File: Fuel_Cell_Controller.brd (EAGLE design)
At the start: 254 x 152.4 mm, 62 parts, among them U1 MAX232PTH

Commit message: lol kk
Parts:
- removed ETH9: ETHERNET, ETHERNET:A122645-ND
- added ETH5: ETHERNET, ETHERNET:A122645-ND
- J1: value (none) -> BLUETOOTH; device SparkFun-Connectors:1X06 -> FCC_parts:1X06BLUETOOTH
- moved H7 568.4 mm to (10.2, 151.1)
- moved H6 530.2 mm to (83.8, 142.2)
- moved H8 486.0 mm to (7.62, 7.62)
- moved H5 408.6 mm to (83.8, 62.2)
- moved H4 319.7 mm to (83.8, 7.62)
- moved R9 309.7 mm to (144.8, 110.5), turned to 180 degrees
- moved R10 306.4 mm to (139.7, 116.8), turned to 270 degrees
- moved R8 305.3 mm to (148.6, 124.5)
- moved R4 304.1 mm to (165.1, 133.3), turned to 270 degrees
- moved R3 303.7 mm to (165.1, 121.9), turned to 90 degrees
- moved J1 303.0 mm to (154.9, 40.6), turned to 180 degrees
- moved R6 295.2 mm to (148.6, 134.6)
- moved R7 294.1 mm to (142.2, 129.5), turned to 90 degrees
- moved R1 290.8 mm to (144.8, 86.4), turned to 180 degrees
- moved U$16 289.2 mm to (153.7, 116.8), turned to 90 degrees
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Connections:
- removed net AGND: ETH1.P$7, ETH4.P$8, J2.1, U$1.AGND, U$19.P$2, X1.2
- removed net ISC1_SCL: SHTSENSOR.3
- removed net ISC1_SDA: SHTSENSOR.4
- net +5V: now also J1.3; no longer J1.4
- net ESTOP_1: now also ETH5.P$3; no longer ETH6.P$3
- net ESTOP_2: now also ETH5.P$4; no longer ETH6.P$4
- net FAN1_PWR: now also ETH6.P$1; no longer ETH7.P$1
- net FAN2_PWR: now also ETH6.P$4; no longer ETH7.P$4
- net FAN3_PWR: now also ETH7.P$1; no longer ETH8.P$1
- net FROM_BLUE: now also J1.4; no longer J1.3
- net GND: now also ETH1.P$7, ETH4.P$8, ETH5.P$13, ETH5.P$14, ETH5.P$5, ETH5.P$6, ETH5.P$7, ETH5.P$8, ETH8.P$2, ETH8.P$4, ETH8.P$6, J1.1, J2.1, U$1.AGND, U$19.P$2, X1.2; no longer ETH6.P$5, ETH6.P$6, ETH6.P$7, ETH9.P$13, ETH9.P$14, ETH9.P$2, ETH9.P$4, ETH9.P$6, ETH9.P$8, J1.6
- net H2_OK: now also ETH5.P$2; no longer ETH6.P$2
- net I2C1_SCL: now also SHTSENSOR.3
- net I2C1_SDA: now also SHTSENSOR.4
- net OUTPUT_1_ENET: now also ETH8.P$5; no longer ETH9.P$5
- net OUTPUT_2_ENET: now also ETH8.P$7; no longer ETH9.P$7
- net PURGE_VALVE_ENET: now also ETH8.P$3; no longer ETH9.P$3
- net PWM_1: now also ETH6.P$3; no longer ETH7.P$3
- net PWM_2: now also ETH6.P$6; no longer ETH7.P$6
- net PWM_3: now also ETH7.P$3; no longer ETH8.P$3
- net STOP: now also ETH5.P$1; no longer ETH6.P$1
- net SUPPLY_VALVE_ENET: now also ETH8.P$1; no longer ETH9.P$1
- net TACH_1: now also ETH6.P$2; no longer ETH7.P$2
- net TACH_2: now also ETH6.P$5; no longer ETH7.P$5
- net TACH_3: now also ETH7.P$2; no longer ETH8.P$2
- net TO_BLUE: now also J1.5; no longer J1.2
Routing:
- added copper zone on layer 1, net GND
- added copper zone on layer 16, net N$15
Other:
- board size 254 x 152.4 mm -> 203.2 x 163.8 mm

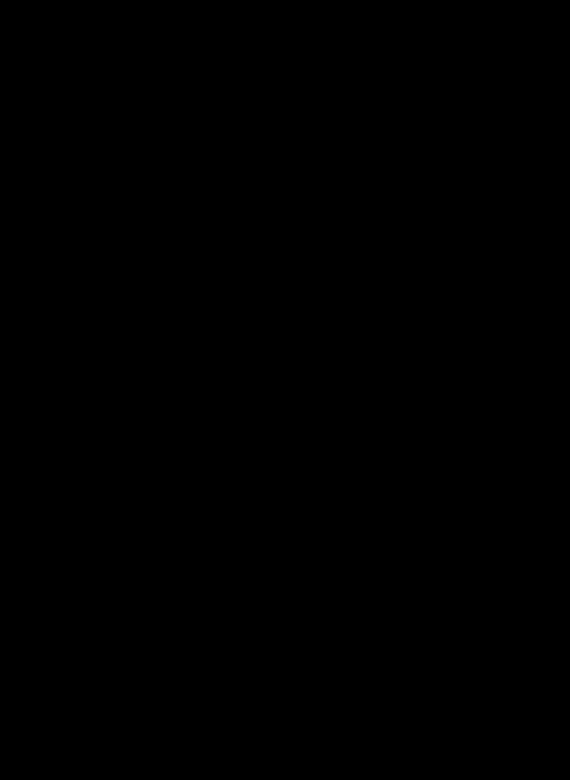
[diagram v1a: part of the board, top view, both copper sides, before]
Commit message: Added a couple of indicator LEDs
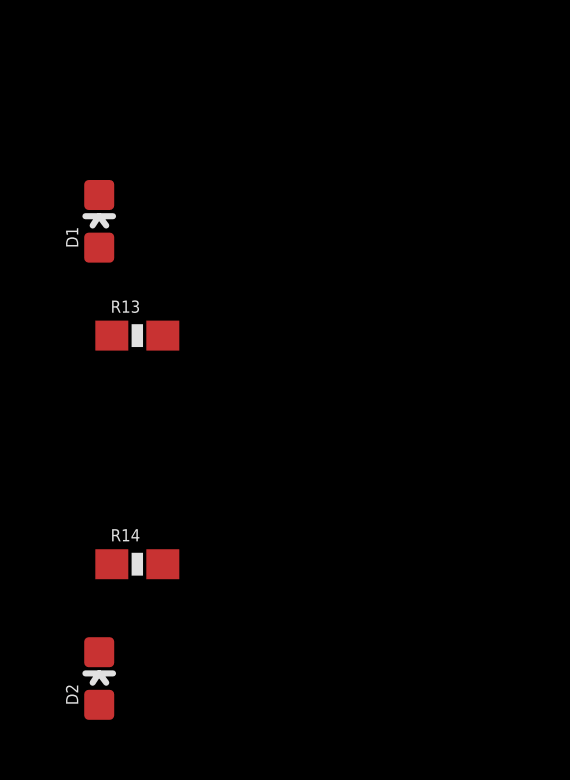
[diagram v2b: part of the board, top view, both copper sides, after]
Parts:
- added D1: BLUE, SparkFun-LED:LED-0603
- added D2: GREEN, SparkFun-LED:LED-0603
- added R13, R14: 249Ω, SparkFun-Resistors:0603-RES
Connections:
- new net N$16: D1.A, R13.2
- new net N$17: D2.A, R14.2
- net +5V: now also R13.1
- net FC5V: now also R14.1
- net GND: now also D1.C, D2.C

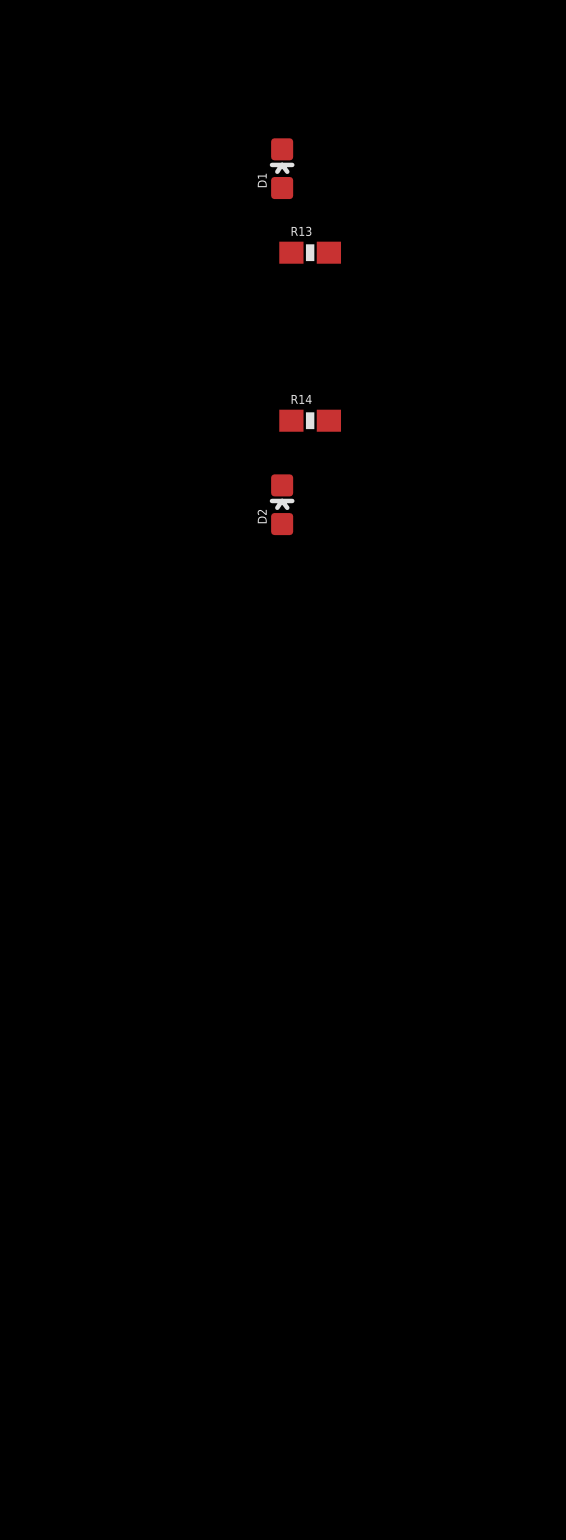
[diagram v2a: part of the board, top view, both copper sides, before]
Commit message: Added TLV2404 Op-amp part (with Dil14 package)
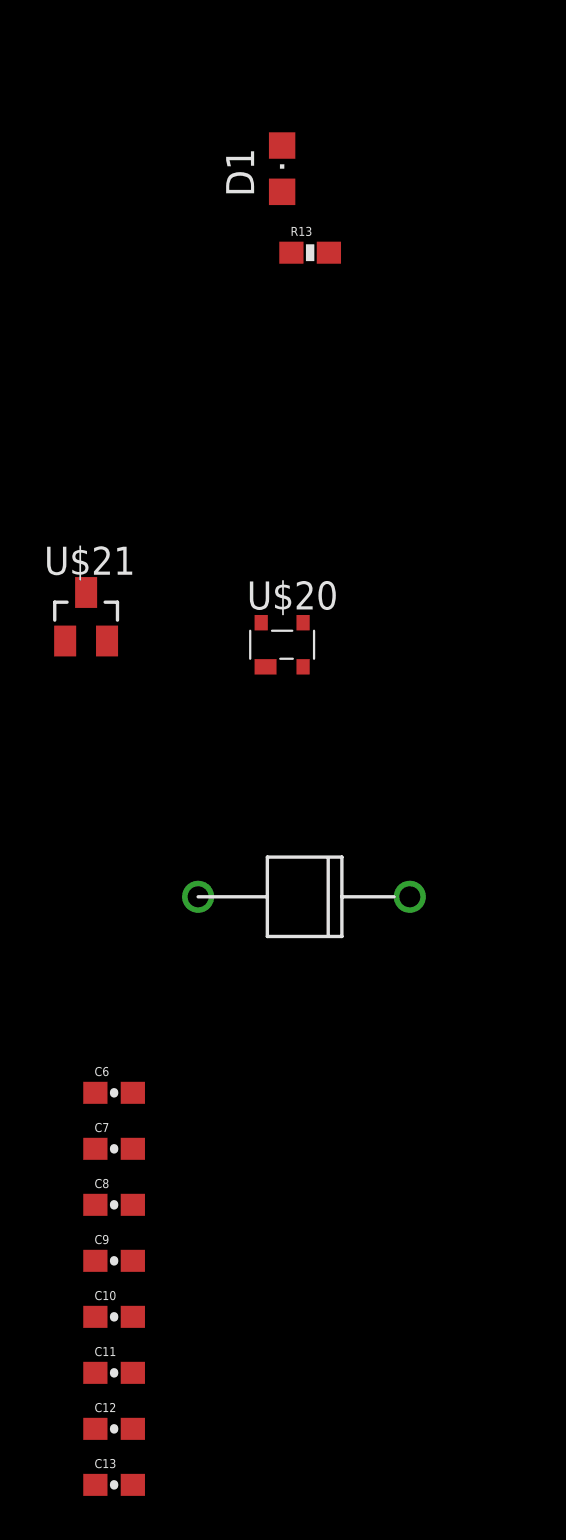
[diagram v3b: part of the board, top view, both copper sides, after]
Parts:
- removed D2: GREEN, SparkFun-LED:LED-0603
- removed R14: 249Ω, SparkFun-Resistors:0603-RES
- added C10, C11, C12, C13, C9: 20µF, SparkFun-Capacitors:0603-CAP
- added C6: 1µF, SparkFun-Capacitors:0603-CAP
- added C7, C8: 5µF, SparkFun-Capacitors:0603-CAP
- added U$20: CD143A-SR3.3CT-ND, 3_3V TVS:SOT143_AVAGO
- added U$21: 641-1198-1-ND, 5V TVS:SOT23
- added U$22: P6KE15A-E3/54GICT-ND, 12V TVS:DO-204AC
- D1: device SparkFun-LED:LED-0603 -> led:CHIPLED_0805
- R13: value 249Ω -> 1kΩ
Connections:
- removed net N$17: D2.A, R14.2
- new net N$18: U$1.PG_0
- new net N$19: U$1.PG_1
- new net N$20: U$1.PG_2
- net +5V: now also C7.1, C8.1, U$21.C
- net 3V3: now also C6.1, U$20.VDD
- net FC12V: now also C10.1, C11.1, C12.1, C13.1, C9.1, U$22.CATHODE
- net FC5V: no longer R14.1
- net GND: now also C10.2, C11.2, C12.2, C13.2, C6.2, C7.2, C8.2, C9.2, U$20.GND, U$21.A1, U$21.A2, U$22.ANODE; no longer D2.C
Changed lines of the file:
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@@
 <element name="H7" library="holes" library_urn="urn:adsk.eagle:library:237" package="3,6-PAD" package3d_urn="urn:adsk.eagle:package:14284/1" value="MOUNT-PAD-ROUND3.6" x="10.16" y="151.13"/>
 <element name="H8" library="holes" library_urn="urn:adsk.eagle:library:237" package="3,6-PAD" package3d_urn="urn:adsk.eagle:package:14284/1" value="MOUNT-PAD-ROUND3.6" x="7.62" y="7.62"/>
-<element name="D1" library="SparkFun-LED" package="LED-0603" value="BLUE" x="-19.05" y="-24.13">
-<attribute name="PROD_ID" value="DIO-08575" x="-19.05" y="-24.13" size="1.778" layer="27" display="off"/>
-</element>
-<element name="R13" library="SparkFun-Resistors" package="0603-RES" value="249Ω" x="-17.78" y="-27.94"/>
-<element name="R14" library="SparkFun-Resistors" package="0603-RES" value="249Ω" x="-17.78" y="-35.56"/>
-<element name="D2" library="SparkFun-LED" package="LED-0603" value="GREEN" x="-19.05" y="-39.37">
-<attribute name="PROD_ID" value="DIO-00821" x="-19.05" y="-39.37" size="1.778" layer="27" display="off"/>
-</element>
+<element name="D1" library="led" library_urn="urn:adsk.eagle:library:259" package="CHIPLED_0805" package3d_urn="urn:adsk.eagle:package:15821/1" value="BLUE" x="-19.05" y="-24.13"/>
+<element name="R13" library="SparkFun-Resistors" package="0603-RES" value="1kΩ" x="-17.78" y="-27.94"/>
+<element name="U$20" library="3_3V TVS" package="SOT143_AVAGO" value="CD143A-SR3.3CT-ND" x="-19.05" y="-45.72"/>
+<element name="U$21" library="5V TVS" package="SOT23" value="641-1198-1-ND" x="-27.94" y="-44.45"/>
+<element name="U$22" library="12V TVS" package="DO-204AC" value="P6KE15A-E3/54GICT-ND" x="-22.86" y="-57.15"/>
+<element name="C6" library="SparkFun-Capacitors" package="0603-CAP" value="1µF" x="-26.67" y="-66.04"/>
+<element name="C7" library="SparkFun-Capacitors" package="0603-CAP" value="5µF" x="-26.67" y="-68.58"/>
+<element name="C8" library="SparkFun-Capacitors" package="0603-CAP" value="5µF" x="-26.67" y="-71.12"/>
+<element name="C9" library="SparkFun-Capacitors" package="0603-CAP" value="20µF" x="-26.67" y="-73.66"/>
+<element name="C10" library="SparkFun-Capacitors" package="0603-CAP" value="20µF" x="-26.67" y="-76.2"/>
+<element name="C11" library="SparkFun-Capacitors" package="0603-CAP" value="20µF" x="-26.67" y="-78.74"/>
+<element name="C12" library="SparkFun-Capacitors" package="0603-CAP" value="20µF" x="-26.67" y="-81.28"/>
+<element name="C13" library="SparkFun-Capacitors" package="0603-CAP" value="20µF" x="-26.67" y="-83.82"/>
 </elements>
 <signals>
@@
 <contactref element="ETH4" pad="P$8"/>
 <contactref element="D1" pad="C"/>
-<contactref element="D2" pad="C"/>
+<contactref element="U$20" pad="GND"/>
+<contactref element="U$21" pad="A1"/>
+<contactref element="U$21" pad="A2"/>
+<contactref element="U$22" pad="ANODE"/>
+<contactref element="C6" pad="2"/>
+<contactref element="C13" pad="2"/>
+<contactref element="C7" pad="2"/>
+<contactref element="C8" pad="2"/>
+<contactref element="C9" pad="2"/>
+<contactref element="C10" pad="2"/>
+<contactref element="C11" pad="2"/>
+<contactref element="C12" pad="2"/>
 <wire x1="107.0864" y1="147.32" x2="113.03" y2="139.7" width="0" layer="19" extent="1-1"/>
 <wire x1="107.95" y1="129.145" x2="113.03" y2="139.7" width="0" layer="19" extent="1-1"/>
@@
 <wire x1="8.89" y1="14.610715625" x2="11.43" y2="14.610715625" width="0" layer="19" extent="1-1"/>
 <wire x1="7.62" y1="7.62" x2="8.89" y2="14.610715625" width="0" layer="19" extent="1-1"/>
-<wire x1="-19.05" y1="-23.253" x2="7.62" y2="7.62" width="0" layer="19" extent="1-1"/>
-<wire x1="-19.05" y1="-38.493" x2="-19.05" y2="-23.253" width="0" layer="19" extent="1-1"/>
+<wire x1="-19.05" y1="-23.08" x2="7.62" y2="7.62" width="0" layer="19" extent="1-1"/>
+<wire x1="-19.8" y1="-46.72" x2="-19.05" y2="-23.08" width="0" layer="19" extent="1-1"/>
+<wire x1="-26.99" y1="-45.55" x2="-19.8" y2="-46.72" width="0" layer="19" extent="1-1"/>
+<wire x1="-28.89" y1="-45.55" x2="-26.99" y2="-45.55" width="0" layer="19" extent="1-1"/>
+<wire x1="-22.86" y1="-57.15" x2="-19.8" y2="-46.72" width="0" layer="19" extent="1-1"/>
+<wire x1="-25.82" y1="-66.04" x2="-22.86" y2="-57.15" width="0" layer="19" extent="1-1"/>
+<wire x1="-25.82" y1="-68.58" x2="-25.82" y2="-66.04" width="0" layer="19" extent="1-1"/>
+<wire x1="-25.82" y1="-71.12" x2="-25.82" y2="-68.58" width="0" layer="19" extent="1-1"/>
+<wire x1="-25.82" y1="-73.66" x2="-25.82" y2="-71.12" width="0" layer="19" extent="1-1"/>
+<wire x1="-25.82" y1="-76.2" x2="-25.82" y2="-73.66" width="0" layer="19" extent="1-1"/>
+<wire x1="-25.82" y1="-78.74" x2="-25.82" y2="-76.2" width="0" layer="19" extent="1-1"/>
+<wire x1="-25.82" y1="-81.28" x2="-25.82" y2="-78.74" width="0" layer="19" extent="1-1"/>
+<wire x1="-25.82" y1="-83.82" x2="-25.82" y2="-81.28" width="0" layer="19" extent="1-1"/>
 </signal>
 <signal name="+5V">
@@
 <contactref element="R2" pad="1"/>
 <contactref element="R13" pad="1"/>
+<contactref element="U$21" pad="C"/>
+<contactref element="C7" pad="1"/>
+<contactref element="C8" pad="1"/>
 <wire x1="107.95" y1="127.395" x2="110.49" y2="139.7" width="0" layer="19" extent="1-1"/>
 <wire x1="110.885" y1="127" x2="107.95" y2="127.395" width="0" layer="19" extent="1-1"/>
@@
 <wire x1="16.51" y1="83.190715625" x2="97.155" y2="81.28" width="0" layer="19" extent="1-1"/>
 <wire x1="-18.63" y1="-27.94" x2="16.51" y2="83.190715625" width="0" layer="19" extent="1-1"/>
+<wire x1="-27.94" y1="-43.35" x2="-18.63" y2="-27.94" width="0" layer="19" extent="1-1"/>
+<wire x1="-27.52" y1="-68.58" x2="-27.94" y2="-43.35" width="0" layer="19" extent="1-1"/>
+<wire x1="-27.52" y1="-71.12" x2="-27.52" y2="-68.58" width="0" layer="19" extent="1-1"/>
 </signal>
 <signal name="FROM_OPEN">
@@
 <contactref element="U$19" pad="P$1"/>
 <contactref element="JP2" pad="6"/>
+<contactref element="U$20" pad="VDD"/>
+<contactref element="C6" pad="1"/>
 <wire x1="113.03" y1="90.17" x2="138.43" y2="91.44" width="0" layer="19" extent="1-1"/>
 <wire x1="105.41" y1="96.52" x2="113.03" y2="90.17" width="0" layer="19" extent="1-1"/>
@@
 <wire x1="82.55" y1="116.84" x2="95.25" y2="111.76" width="0" layer="19" extent="1-1"/>
 <wire x1="16.51" y1="85.730715625" x2="82.55" y2="116.84" width="0" layer="19" extent="1-1"/>
+<wire x1="-18.1" y1="-44.72" x2="16.51" y2="85.730715625" width="0" layer="19" extent="1-1"/>
+<wire x1="-27.52" y1="-66.04" x2="-18.1" y2="-44.72" width="0" layer="19" extent="1-1"/>
 </signal>
 <signal name="OPEN_RST">
@@
 <contactref element="U$9" pad="D"/>
 <contactref element="R4" pad="1"/>
+<contactref element="U$22" pad="CATHODE"/>
+<contactref element="C9" pad="1"/>
+<contactref element="C13" pad="1"/>
+<contactref element="C12" pad="1"/>
+<contactref element="C11" pad="1"/>
+<contactref element="C10" pad="1"/>
 <wire x1="67.31" y1="144.78" x2="71.12" y2="147.32" width="0" layer="19" extent="1-1"/>
 <wire x1="138.6332" y1="147.32" x2="71.12" y2="147.32" width="0" layer="19" extent="1-1"/>
@@
 <wire x1="16.51" y1="75.570715625" x2="67.31" y2="144.78" width="0" layer="19" extent="1-1"/>
 <wire x1="191.77" y1="16.28" x2="158.75" y2="115.99" width="0" layer="19" extent="1-1"/>
+<wire x1="-13.26" y1="-57.15" x2="16.51" y2="75.570715625" width="0" layer="19" extent="1-1"/>
+<wire x1="-27.52" y1="-73.66" x2="-13.26" y2="-57.15" width="0" layer="19" extent="1-1"/>
+<wire x1="-27.52" y1="-76.2" x2="-27.52" y2="-73.66" width="0" layer="19" extent="1-1"/>
+<wire x1="-27.52" y1="-78.74" x2="-27.52" y2="-76.2" width="0" layer="19" extent="1-1"/>
+<wire x1="-27.52" y1="-81.28" x2="-27.52" y2="-78.74" width="0" layer="19" extent="1-1"/>
+<wire x1="-27.52" y1="-83.82" x2="-27.52" y2="-81.28" width="0" layer="19" extent="1-1"/>
 </signal>
 <signal name="N$3">
@@
 <contactref element="ETH2" pad="P$1"/>
 <contactref element="ETH3" pad="P$7"/>
-<contactref element="R14" pad="1"/>
 <wire x1="191.77" y1="40.41" x2="191.77" y2="58.42" width="0" layer="19" extent="1-1"/>
 <wire x1="69.85" y1="144.78" x2="191.77" y2="58.42" width="0" layer="19" extent="1-1"/>
 <wire x1="68.58" y1="147.32" x2="69.85" y2="144.78" width="0" layer="19" extent="1-1"/>
-<wire x1="-18.63" y1="-35.56" x2="69.85" y2="144.78" width="0" layer="19" extent="1-1"/>
 </signal>
 <signal name="FAN1_PWR">
@@
 <contactref element="R13" pad="2"/>
 <contactref element="D1" pad="A"/>
-<wire x1="-19.05" y1="-25.007" x2="-16.93" y2="-27.94" width="0" layer="19" extent="1-1"/>
-</signal>
-<signal name="N$17">
-<contactref element="R14" pad="2"/>
-<contactref element="D2" pad="A"/>
-<wire x1="-16.93" y1="-35.56" x2="-19.05" y2="-40.247" width="0" layer="19" extent="1-1"/>
+<wire x1="-19.05" y1="-25.18" x2="-16.93" y2="-27.94" width="0" layer="19" extent="1-1"/>
+</signal>
+<signal name="N$18">
+<contactref element="U$1" pad="PG_0"/>
+</signal>
+<signal name="N$19">
+<contactref element="U$1" pad="PG_1"/>
+</signal>
+<signal name="N$20">
+<contactref element="U$1" pad="PG_2"/>
 </signal>
 </signals>

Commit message: Changed resistors and caps to 0805; need to spec out some decoupling capacitors, add LED's, and complete low-pass filter with op-amp
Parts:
- added C14, C15: 0.1µF, SparkFun-Passives:0805
- added R14, R15, R16, R17: 10kΩ, SparkFun-Passives:0805
- added U$23: TLV2404TLV2404, FCC_parts:DIL14
- added U$24: DMP3056L-7DMP3056L-7, FCC_parts:DMP3056L-7
- C1, C2, C3, C4, C5: device rcl:C0603K -> SparkFun-Passives:0805
- D1: value BLUE -> RED; device led:CHIPLED_0805 -> SparkFun-LED:LED-1206
- R1, R10, R11, R12, R2, R3, R4, R5, R6, R7, R8, R9: device SparkFun-Resistors:0603-RES -> SparkFun-Passives:0805
- R13: value 1kΩ -> 324Ω; device SparkFun-Resistors:0603-RES -> SparkFun-Passives:0805
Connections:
- net N$18 renamed RUN_MODE
- new net DEBUG_MODE: U$1.PG_3
- new net INTERRUPT: U$1.PH_0, U$1.PH_1
- new net OE*: R14.1, R15.1, R17.2, U$24.S, U$3.19, U$5.19
- net +5V: now also C14.1, C15.1, R14.2, R15.2; no longer R13.1
- net 3V3: now also R13.1, R16.1, U$24.D
- net GND: now also C14.2, C15.2, R17.1, U$3.11, U$3.12, U$3.13, U$3.7, U$3.8, U$3.9, U$5.11, U$5.9
- net STOP: now also R16.2, U$24.G
